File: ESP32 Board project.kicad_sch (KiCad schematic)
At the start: 26 parts, among them J1 SS-52400-002, J2 B2B-PH-SM4-TB, U1 MCP73871-2CAI_ML

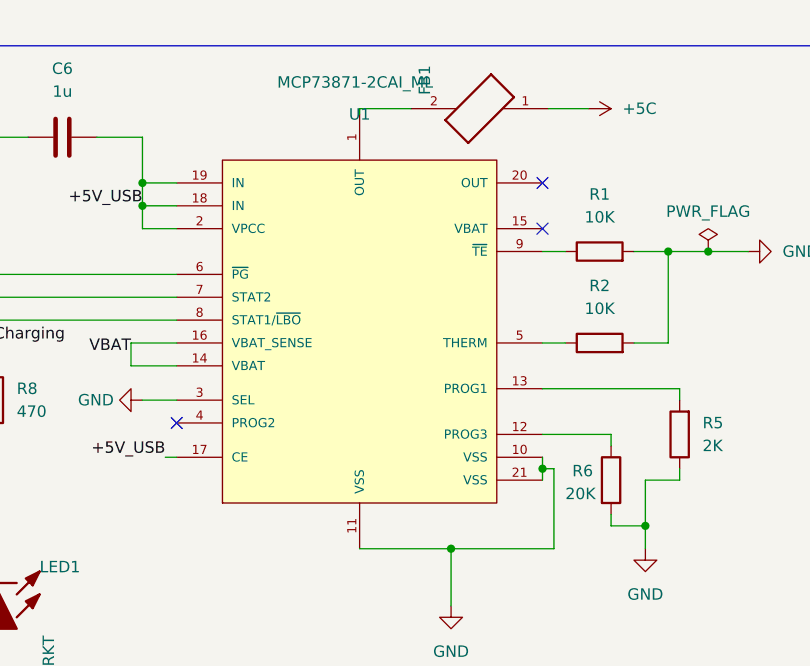
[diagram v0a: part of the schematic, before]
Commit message: Updated SPI connection and +5V connection
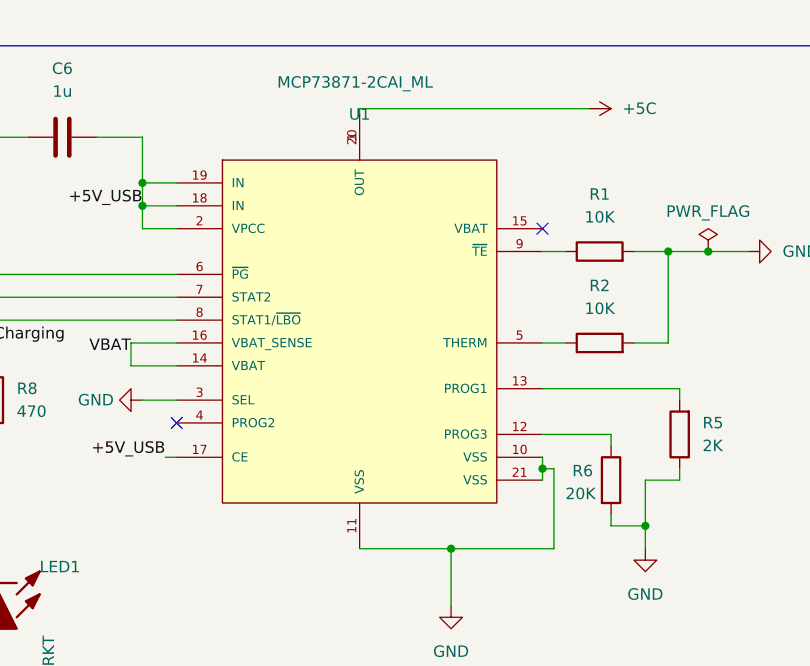
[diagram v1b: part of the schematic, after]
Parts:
- removed FB1: FBMJ2125HM330-T, Footprints:BEADC2012X105N, symbol FBMJ2125HM330-T:FBMJ2125HM330-T
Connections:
- net +5C: now also U1.1 (OUT), U1.20 (OUT)
- no-connect marks 13 -> 12
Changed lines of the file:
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@@
 	)
 	(no_connect
-		(at 245.11 31.75)
-	)
-	(no_connect
 		(at 48.26 60.325)
 	)
@@
 	(wire
 		(pts
-			(xy 245.745 23.495) (xy 250.19 23.495)
-		)
-		(stroke
-			(width 0)
-			(type default)
-		)
-	)
-	(wire
-		(pts
 			(xy 95.25 67.945) (xy 99.06 67.945)
 		)
@@
 	(wire
 		(pts
-			(xy 224.79 23.495) (xy 230.505 23.495)
+			(xy 224.79 23.495) (xy 250.19 23.495)
 		)
 		(stroke
@@
 					(unit 1)
 				)
-			)
-		)
-	)
-	(symbol
-		(lib_id "FBMJ2125HM330-T:FBMJ2125HM330-T")
-		(at 238.125 23.495 180)
-		(unit 1)
-		(exclude_from_sim no)
-		(in_bom yes)
-		(on_board yes)
-		(dnp no)
-		(property "Reference" "FB1"
-			(at 232.029 21.971 90)
-			(effects
-				(font
-					(size 1.27 1.27)
-				)
-				(justify right)
-			)
-		)
-		(property "Value" "FBMJ2125HM330-T"
-			(at 235.077 18.161 0)
-			(effects
-				(font
-					(size 1.27 1.27)
-				)
-				(justify right)
-				(hide yes)
-			)
-		)
-		(property "Footprint" "Footprints:BEADC2012X105N"
-			(at 238.125 23.495 0)
-			(effects
-				(font
-					(size 1.27 1.27)
-				)
-				(justify bottom)
-				(hide yes)
-			)
-		)
-		(property "Datasheet" ""
-			(at 238.125 23.495 0)
-			(effects
-				(font
-					(size 1.27 1.27)
-				)
-				(hide yes)
-			)
-		)
-		(property "Description" ""
-			(at 238.125 23.495 0)
-			(effects
-				(font
-					(size 1.27 1.27)
-				)
-				(hide yes)
-			)
-		)
-		(property "MF" "Taiyo Yuden"
-			(at 238.125 23.495 0)
-			(effects
-				(font
-					(size 1.27 1.27)
-				)
-				(justify bottom)
-				(hide yes)
-			)
-		)
-		(property "Description_1" "33 Ohms @ 100 MHz 1 Power Line Ferrite Bead 0805 (2012 Metric) 4A 8mOhm"
-			(at 238.125 23.495 0)
-			(effects
-				(font
-					(size 1.27 1.27)
-				)
-				(justify bottom)
-				(hide yes)
-			)
-		)
-		(property "Package" "2012 Taiyo Yuden"
-			(at 238.125 23.495 0)
-			(effects
-				(font
-					(size 1.27 1.27)
-				)
-				(justify bottom)
-				(hide yes)
-			)
-		)
-		(property "Price" "None"
-			(at 238.125 23.495 0)
-			(effects
-				(font
-					(size 1.27 1.27)
-				)
-				(justify bottom)
-				(hide yes)
-			)
-		)
-		(property "SnapEDA_Link" "https://www.snapeda.com/parts/FBMJ2125HM330-T/Taiyo+Yuden/view-part/?ref=snap"
-			(at 238.125 23.495 0)
-			(effects
-				(font
-					(size 1.27 1.27)
-				)
-				(justify bottom)
-				(hide yes)
-			)
-		)
-		(property "MP" "FBMJ2125HM330-T"
-			(at 238.125 23.495 0)
-			(effects
-				(font
-					(size 1.27 1.27)
-				)
-				(justify bottom)
-				(hide yes)
-			)
-		)
-		(property "Availability" "In Stock"
-			(at 238.125 23.495 0)
-			(effects
-				(font
-					(size 1.27 1.27)
-				)
-				(justify bottom)
-				(hide yes)
-			)
-		)
-		(property "Check_prices" "https://www.snapeda.com/parts/FBMJ2125HM330-T/Taiyo+Yuden/view-part/?ref=eda"
-			(at 238.125 23.495 0)
-			(effects
-				(font
-					(size 1.27 1.27)
-				)
-				(justify bottom)
-				(hide yes)
-			)
-		)
-		(pin "1"
-		)
-		(pin "2"
-		)
-		(instances
-			(project "ESP32 Board project"
-				(path "/c99d1e6a-506e-41b0-84a4-68868b057b95"
-					(reference "FB1")
-					(unit 1)
-				)
